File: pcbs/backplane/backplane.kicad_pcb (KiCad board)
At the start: 2 copper layers, 80 x 50 mm, 192 parts, among them J1 CONN_01X04, P1 USB_B, P2 CONN_01X03, P3 CONN_02X03, P4 CONN_02X03, P5 CONN_02X07, P6 CONN_02X07, P7 CONN_01X03, P8 CONN_01X03, Q1 MMBT3904, Q2 MMBT3904, Q3 Si2323, U1 LM358, U2 TC1262-33VDB, U3 LM358, U4 CH340G, Y1 Crystal

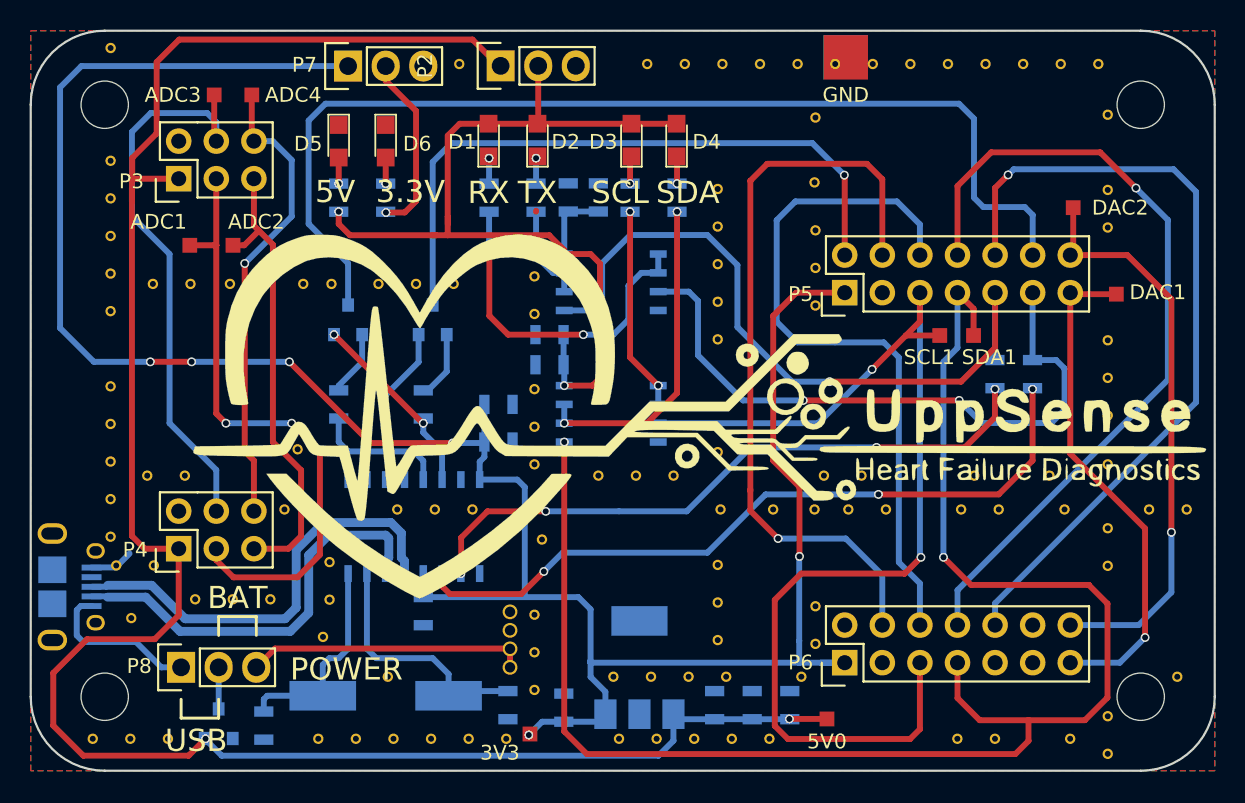
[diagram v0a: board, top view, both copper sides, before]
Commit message: Finished the photo extender, backplane and the analog board.
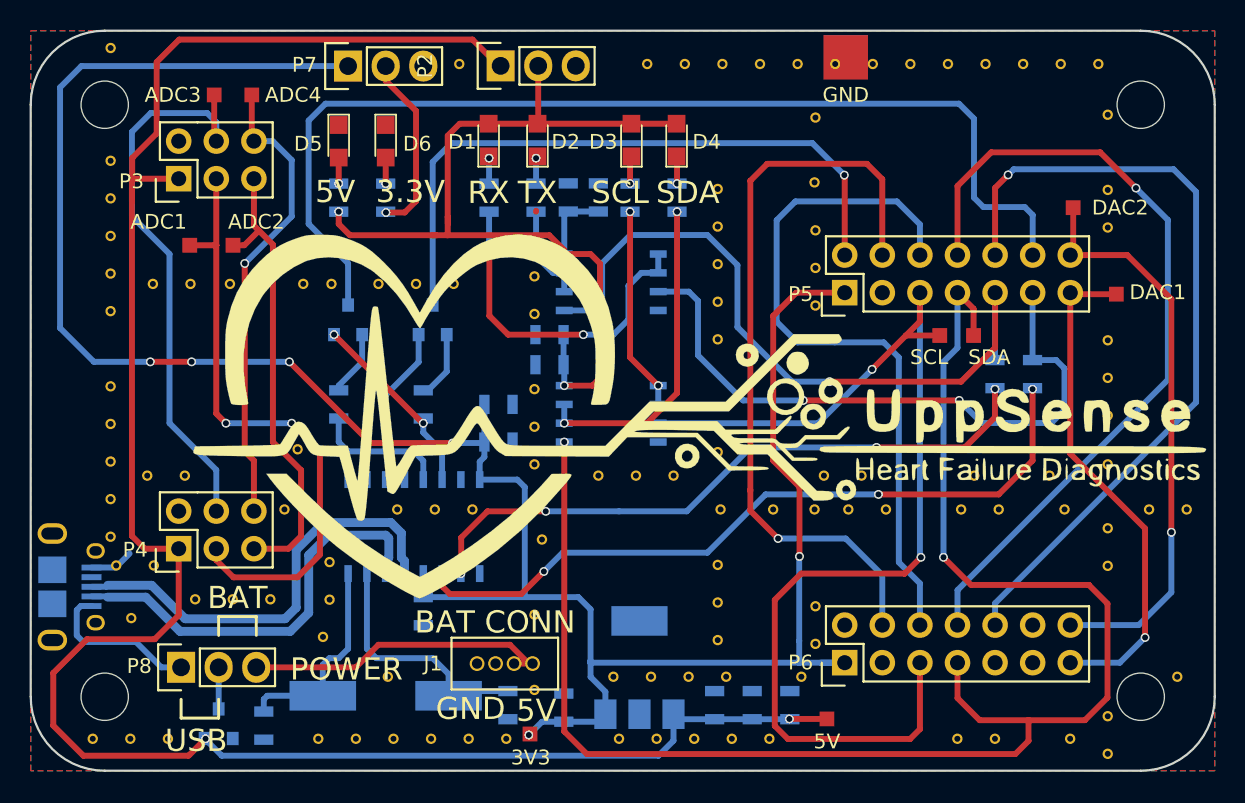
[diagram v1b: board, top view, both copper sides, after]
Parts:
- removed the REF** at (148.5, 108.2)
- J1: moved to F.Cu
- moved J1 1.55 mm to (148.4, 109.0), turned to 270 degrees
- renumbered 5V0 to 5V, SCL1 to SCL, SDA1 to SDA
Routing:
- net 5V_BATT: track 18.9 -> 21.1 mm
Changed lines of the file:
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@@
 (kicad_pcb (version 4) (host pcbnew 4.0.6-e0-6349~52~ubuntu17.04.1)
   (general
-    (links 253)
+    (links 252)
     (no_connects 0)
     (area 114.400999 66.146999 194.551001 116.297001)
     (thickness 1.6)
     (drawings 41)
-    (tracks 499)
+    (tracks 501)
     (zones 0)
-    (modules 192)
+    (modules 191)
     (nets 45)
   )
   (page A4)
   (title_block
-    (title "Backplane for UppSense")
-    (date 2017-06-20)
-    (rev 1.0)
-    (company "Uppsala University")
+    (title "Backplane UppSense 2017")
+    (date 2017-07-05)
+    (rev v0.1)
+    (company "UppSense Heart Failure Diagnostics")
   )
   (layers
@@
     (34 B.Paste user)
     (35 F.Paste user)
-    (36 B.SilkS user hide)
+    (36 B.SilkS user)
     (37 F.SilkS user)
     (38 B.Mask user)
@@
   )
   (module myVias:Stitchging-Via-0.4-0.7 (layer F.Cu)
-    (at 148.512 108.221 180)
-    (fp_text reference REF** (at 0 1.27 180) (layer F.SilkS) hide
-      (effects (font (size 1 1) (thickness 0.15)))
-    )
-    (fp_text value Stitching-Via-0.4-0.7 (at 0 -1.27 180) (layer F.Fab) hide
-      (effects (font (size 1 1) (thickness 0.15)))
-    )
-    (pad ~ thru_hole circle (at 0 0 180) (size 0.7 0.7) (drill 0.4) (layers *.Cu)
-      (net 1 GND) (zone_connect 2))
-  )
-  (module myVias:Stitchging-Via-0.4-0.7 (layer F.Cu)
     (at 148.512 105.681 180)
     (fp_text reference REF** (at 0 1.27 180) (layer F.SilkS) hide
@@
   (module myTestPoints:TP_SMD_quadr_1mm (layer F.Cu)
     (at 175.895 86.816)
-    (fp_text reference SCL1 (at -0.713 1.466) (layer F.SilkS)
+    (fp_text reference SCL (at -0.713 1.466) (layer F.SilkS)
       (effects (font (size 1 1) (thickness 0.15)))
     )
@@
   (module myTestPoints:TP_SMD_quadr_1mm (layer F.Cu)
     (at 178.181 86.816)
-    (fp_text reference SDA1 (at 1.065 1.466) (layer F.SilkS)
+    (fp_text reference SDA (at 1.065 1.466) (layer F.SilkS)
       (effects (font (size 1 1) (thickness 0.15)))
     )
@@
   (module myTestPoints:TP_SMD_quadr_1mm (layer F.Cu)
     (at 168.275 112.724)
-    (fp_text reference 5V0 (at 0 1.524) (layer F.SilkS)
+    (fp_text reference 5V (at 0 1.524) (layer F.SilkS)
       (effects (font (size 1 1) (thickness 0.15)))
     )
@@
   (module myTestPoints:TP_SMD_quadr_1mm (layer F.Cu)
     (at 148.209 113.74)
-    (fp_text reference 3V3 (at -2.032 1.27) (layer F.SilkS)
+    (fp_text reference 3V3 (at 0.049 1.593) (layer F.SilkS)
       (effects (font (size 1 1) (thickness 0.15)))
     )
@@
     (pad 1 np_thru_hole circle (at 0 0) (size 3.2 3.2) (drill 3.2) (layers *.Cu *.Mask))
   )
-  (module ConnectorsChina:LED_CONN_1.25_PITCH (layer B.Cu)
-    (at 146.861 109.237)
-    (fp_text reference J1 (at 0 -6.7 180) (layer B.SilkS)
-      (effects (font (size 1 1) (thickness 0.15)) (justify mirror))
+  (module ConnectorsChina:LED_CONN_1.25_PITCH (layer F.Cu)
+    (at 148.385 108.983 270)
+    (fp_text reference J1 (at 0 6.731 540) (layer F.SilkS)
+      (effects (font (size 1 1) (thickness 0.15)))
     )
-    (fp_text value CONN_01X04 (at 0 2.6) (layer B.Fab)
-      (effects (font (size 1 1) (thickness 0.15)) (justify mirror))
+    (fp_text value CONN_01X04 (at 0 -2.6 270) (layer F.Fab)
+      (effects (font (size 1 1) (thickness 0.15)))
     )
-    (fp_line (start 1.75 1.725) (end 1.75 -5.475) (layer B.SilkS) (width 0.15))
-    (fp_line (start -1.75 1.725) (end -1.75 -5.475) (layer B.SilkS) (width 0.15))
-    (fp_line (start -1.75 -5.475) (end 1.75 -5.475) (layer B.SilkS) (width 0.15))
-    (fp_line (start -1.75 1.725) (end 1.75 1.725) (layer B.SilkS) (width 0.15))
-    (pad 4 thru_hole circle (at 0 -3.75) (size 1 1) (drill 0.7) (layers *.Cu *.Mask B.SilkS)
+    (fp_line (start 1.75 -1.725) (end 1.75 5.475) (layer F.SilkS) (width 0.15))
+    (fp_line (start -1.75 -1.725) (end -1.75 5.475) (layer F.SilkS) (width 0.15))
+    (fp_line (start -1.75 5.475) (end 1.75 5.475) (layer F.SilkS) (width 0.15))
+    (fp_line (start -1.75 -1.725) (end 1.75 -1.725) (layer F.SilkS) (width 0.15))
+    (pad 4 thru_hole circle (at 0 3.75 270) (size 1 1) (drill 0.7) (layers *.Cu *.Mask F.SilkS)
       (net 1 GND))
-    (pad 3 thru_hole circle (at 0 -2.5) (size 1 1) (drill 0.7) (layers *.Cu *.Mask B.SilkS)
+    (pad 3 thru_hole circle (at 0 2.5 270) (size 1 1) (drill 0.7) (layers *.Cu *.Mask F.SilkS)
       (net 1 GND))
-    (pad 1 thru_hole circle (at 0 0) (size 1 1) (drill 0.7) (layers *.Cu *.Mask B.SilkS)
+    (pad 1 thru_hole circle (at 0 0 270) (size 1 1) (drill 0.7) (layers *.Cu *.Mask F.SilkS)
       (net 40 5V_BATT))
-    (pad 2 thru_hole circle (at 0 -1.25) (size 1 1) (drill 0.7) (layers *.Cu *.Mask B.SilkS)
+    (pad 2 thru_hole circle (at 0 1.25 270) (size 1 1) (drill 0.7) (layers *.Cu *.Mask F.SilkS)
       (net 40 5V_BATT))
   )
@@
     (arrow2b (pts (xy 119.476 119.222) (xy 118.349496 119.808421)))
   )
-  (gr_text "BAT CONN" (at 155.37 101.998) (layer B.SilkS)
-    (effects (font (size 1.5 1.5) (thickness 0.3)) (justify mirror))
+  (gr_text "BAT CONN" (at 145.845 106.189) (layer F.SilkS)
+    (effects (font (size 1.5 1.5) (thickness 0.3)))
   )
-  (gr_text GND (at 151.052 105.808) (layer B.SilkS)
-    (effects (font (size 1.5 1.5) (thickness 0.3)) (justify mirror))
+  (gr_text GND (at 144.194 112.031) (layer F.SilkS)
+    (effects (font (size 1.5 1.5) (thickness 0.3)))
   )
-  (gr_text 5V (at 150.798 108.602) (layer B.SilkS)
-    (effects (font (size 1.5 1.5) (thickness 0.3)) (justify mirror))
+  (gr_text 5V (at 148.639 112.158) (layer F.SilkS)
+    (effects (font (size 1.5 1.5) (thickness 0.3)))
   )
   (gr_text POWER (at 135.812 109.364) (layer F.SilkS)
@@
   (segment (start 158.146 74.792) (end 158.146 76.552) (width 0.4) (layer F.Cu) (net 39))
   (via (at 158.146 76.552) (size 0.6) (drill 0.4) (layers F.Cu B.Cu) (net 39))
-  (segment (start 146.861 109.237) (end 146.861 107.987) (width 0.4) (layer F.Cu) (net 40))
-  (segment (start 146.861 107.987) (end 146.841 107.967) (width 0.4) (layer F.Cu) (net 40))
-  (segment (start 146.841 107.967) (end 130.986 107.967) (width 0.4) (layer F.Cu) (net 40))
-  (segment (start 130.986 107.967) (end 129.716 109.237) (width 0.4) (layer F.Cu) (net 40))
+  (segment (start 129.716 109.237) (end 136.447 109.237) (width 0.4) (layer F.Cu) (net 40))
+  (segment (start 146.861 107.713) (end 148.131 108.983) (width 0.4) (layer F.Cu) (net 40))
+  (segment (start 137.971 107.713) (end 146.861 107.713) (width 0.4) (layer F.Cu) (net 40))
+  (segment (start 136.447 109.237) (end 137.971 107.713) (width 0.4) (layer F.Cu) (net 40))
+  (segment (start 148.131 108.983) (end 148.385 108.983) (width 0.4) (layer F.Cu) (net 40))
+  (segment (start 148.385 108.983) (end 147.135 108.983) (width 0.4) (layer F.Cu) (net 40))
   (segment (start 124.636 109.237) (end 123.3025 109.237) (width 0.4) (layer B.Cu) (net 41))
   (segment (start 117.861 105.09) (end 118.601 105.09) (width 0.4) (layer B.Cu) (net 41))

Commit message: Added BOMs and gerber files.
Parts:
- added J2: CONN_01X01, mySamtec:Samtec-PHT-1-1-01-L-S, F.Cu at (183.3, 71.5)
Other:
- board text added: "HOUSING GND"
- board text added: "LED CONTROL"
- board text added: "OFF"
- board text added: "ON"
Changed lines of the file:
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@@
 (kicad_pcb (version 4) (host pcbnew 4.0.6-e0-6349~52~ubuntu17.04.1)
   (general
-    (links 252)
+    (links 253)
     (no_connects 0)
     (area 114.400999 66.146999 194.551001 116.297001)
     (thickness 1.6)
-    (drawings 41)
+    (drawings 51)
     (tracks 501)
     (zones 0)
-    (modules 191)
+    (modules 192)
     (nets 45)
   )
@@
   )
   (setup
-    (last_trace_width 0.4)
+    (last_trace_width 0.25)
     (user_trace_width 0.2)
     (user_trace_width 0.3)
@@
     (visible_elements FFFFFFDF)
     (pcbplotparams
-      (layerselection 0x00030_80000001)
+      (layerselection 0x010f0_80000001)
       (usegerberextensions false)
       (excludeedgelayer true)
@@
       (outputformat 1)
       (mirror false)
-      (drillshape 1)
+      (drillshape 0)
       (scaleselection 1)
-      (outputdirectory ""))
+      (outputdirectory /home/maximilian/UppSense/pcbs/backplane/output/gerber/))
   )
   (net 0 "")
@@
     (descr Samtec-PHT-1-3-01-L-S)
     (tags "pin header")
-    (fp_text reference P7 (at 0.084 -2.952 180) (layer F.SilkS)
+    (fp_text reference P7 (at -0.874 -2.776 180) (layer F.SilkS)
       (effects (font (size 1 1) (thickness 0.15)))
     )
@@
   (module myTestPoints:TP_SMD_quadr_1mm (layer F.Cu)
     (at 129.413 70.56)
-    (fp_text reference ADC4 (at 2.794 0) (layer F.SilkS)
+    (fp_text reference ADC4 (at 0.049 -1.328) (layer F.SilkS)
       (effects (font (size 1 1) (thickness 0.15)))
     )
@@
     (descr Samtec-PHT-1-3-01-L-S)
     (tags "pin header")
-    (fp_text reference P2 (at 0 -5.1 90) (layer F.SilkS)
+    (fp_text reference P2 (at 0 -2.667 180) (layer F.SilkS)
       (effects (font (size 1 1) (thickness 0.15)))
     )
@@
       (net 1 GND))
   )
+  (module mySamtec:Samtec-PHT-1-1-01-L-S (layer F.Cu)
+    (at 183.31 71.518)
+    (descr "Through hole straight pin header, 1x01, 2.54mm pitch, single row")
+    (tags "Through hole pin header THT 1x01 2.54mm single row")
+    (fp_text reference J2 (at 0 -2.39) (layer F.SilkS)
+      (effects (font (size 1 1) (thickness 0.15)))
+    )
+    (fp_text value CONN_01X01 (at 0 2.39) (layer F.Fab)
+      (effects (font (size 1 1) (thickness 0.15)))
+    )
+    (fp_line (start -1.27 -1.27) (end -1.27 1.27) (layer F.Fab) (width 0.1))
+    (fp_line (start -1.27 1.27) (end 1.27 1.27) (layer F.Fab) (width 0.1))
+    (fp_line (start 1.27 1.27) (end 1.27 -1.27) (layer F.Fab) (width 0.1))
+    (fp_line (start 1.27 -1.27) (end -1.27 -1.27) (layer F.Fab) (width 0.1))
+    (fp_line (start -1.39 1.27) (end -1.39 1.39) (layer F.SilkS) (width 0.12))
+    (fp_line (start -1.39 1.39) (end 1.39 1.39) (layer F.SilkS) (width 0.12))
+    (fp_line (start 1.39 1.39) (end 1.39 1.27) (layer F.SilkS) (width 0.12))
+    (fp_line (start 1.39 1.27) (end -1.39 1.27) (layer F.SilkS) (width 0.12))
+    (fp_line (start -1.39 0) (end -1.39 -1.39) (layer F.SilkS) (width 0.12))
+    (fp_line (start -1.39 -1.39) (end 0 -1.39) (layer F.SilkS) (width 0.12))
+    (fp_line (start -1.6 -1.6) (end -1.6 1.6) (layer F.CrtYd) (width 0.05))
+    (fp_line (start -1.6 1.6) (end 1.6 1.6) (layer F.CrtYd) (width 0.05))
+    (fp_line (start 1.6 1.6) (end 1.6 -1.6) (layer F.CrtYd) (width 0.05))
+    (fp_line (start 1.6 -1.6) (end -1.6 -1.6) (layer F.CrtYd) (width 0.05))
+    (pad 1 thru_hole rect (at 0 0) (size 2.1 1.9) (drill 1.2) (layers *.Cu *.Mask)
+      (net 1 GND))
+    (model Pin_Headers.3dshapes/Pin_Header_Straight_1x01_Pitch2.54mm.wrl
+      (at (xyz 0 0 0))
+      (scale (xyz 1 1 1))
+      (rotate (xyz 0 0 90))
+    )
+  )
+  (gr_text OFF (at 152.068 71.518) (layer F.SilkS)
+    (effects (font (size 1.5 1.5) (thickness 0.3)))
+  )
+  (gr_text ON (at 132.891 71.518) (layer F.SilkS)
+    (effects (font (size 1.5 1.5) (thickness 0.3)))
+  )
+  (gr_line (start 138.479 71.264) (end 138.479 70.502) (angle 90) (layer F.SilkS) (width 0.2))
+  (gr_line (start 135.812 71.264) (end 138.479 71.264) (angle 90) (layer F.SilkS) (width 0.2))
+  (gr_line (start 135.812 70.502) (end 135.812 71.264) (angle 90) (layer F.SilkS) (width 0.2))
+  (gr_line (start 148.766 71.264) (end 148.766 70.502) (angle 90) (layer F.SilkS) (width 0.2))
+  (gr_line (start 145.972 71.264) (end 148.766 71.264) (angle 90) (layer F.SilkS) (width 0.2))
+  (gr_line (start 145.972 70.502) (end 145.972 71.264) (angle 90) (layer F.SilkS) (width 0.2))
+  (gr_text "LED CONTROL" (at 125.271 67.708) (layer F.SilkS)
+    (effects (font (size 1.5 1.5) (thickness 0.3)))
+  )
+  (gr_text "HOUSING GND" (at 183.31 75.328) (layer F.SilkS)
+    (effects (font (size 1.5 1.5) (thickness 0.3)))
+  )
   (dimension 5 (width 0.3) (layer Dwgs.User)
